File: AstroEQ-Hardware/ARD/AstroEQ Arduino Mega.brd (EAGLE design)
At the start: 101.6 x 53.3 mm, 19 parts, among them J1 POWER_JACKPTH, M0 Motor Driver, M1 Motor Driver

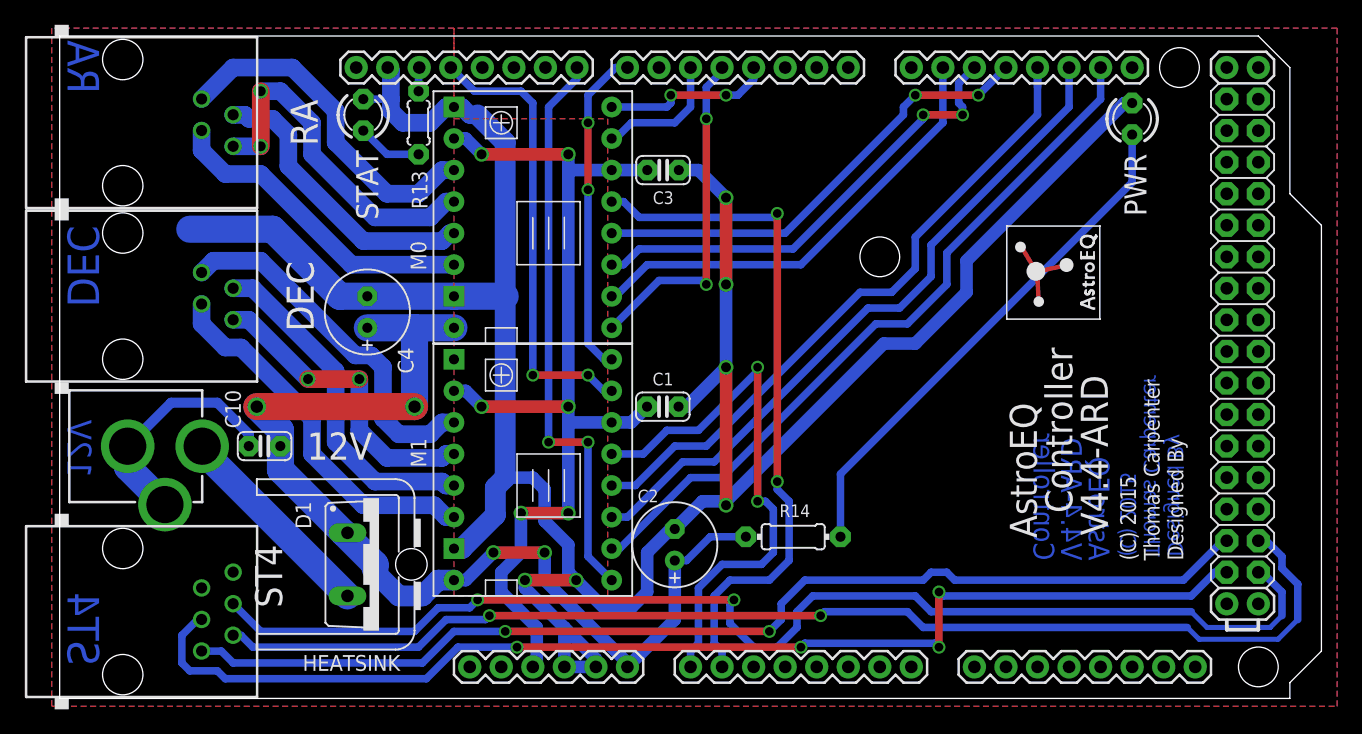
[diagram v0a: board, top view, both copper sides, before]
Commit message: Update Arduino Mega PCB design to V4.8
Adds:
* Speed control line to ST4 connector
* DRV8834 support using 3-pin jumper selection headers.
* PWM output connector jack
* IO header for target speed selection, emergency stop, and snap pin.
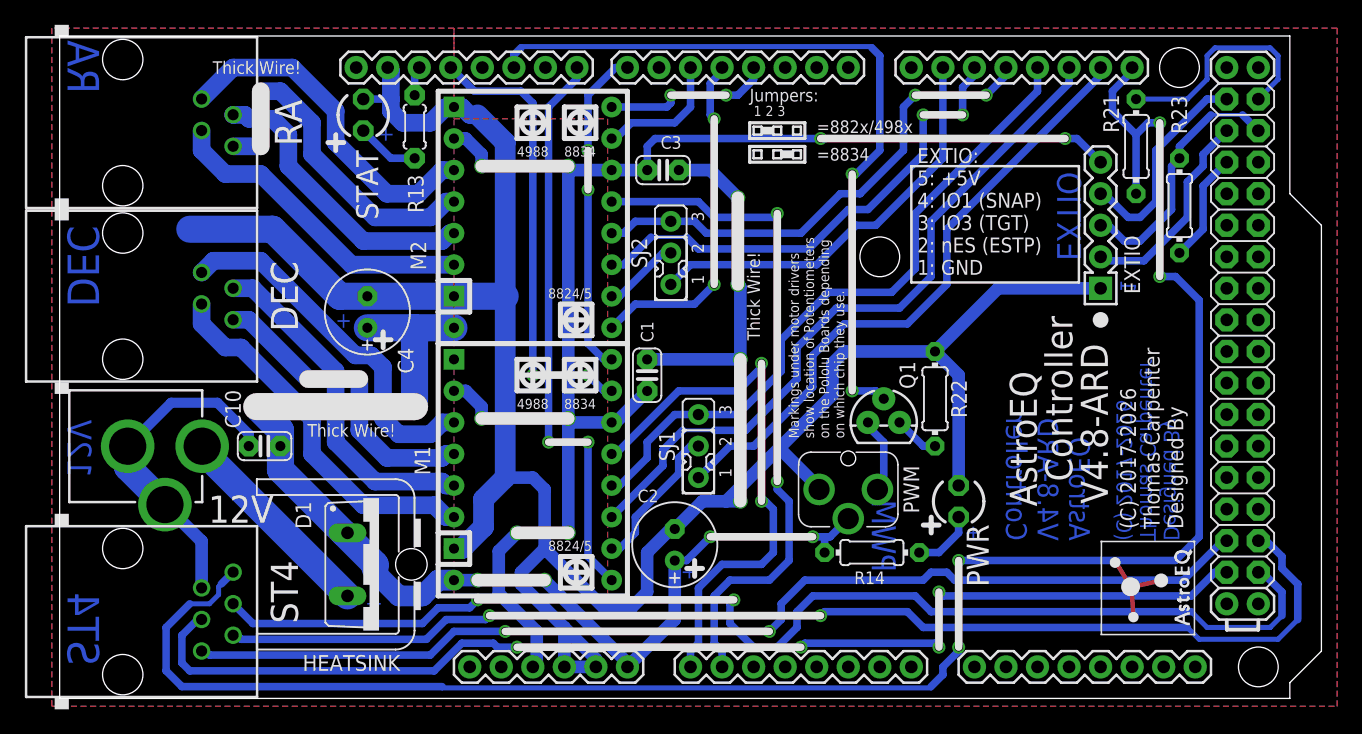
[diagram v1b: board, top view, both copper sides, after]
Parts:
- added EXTIO: 5pin HDR, SparkFun:1X05
- added J2, J3: DNI, jumper:JUMP
- added PWM: JACK, SparkFun:AUDIO-JACK-3.5MM-VERT
- added Q1: BS270, SparkFun:TO-92
- added R21, R23: 1k, rcl:0204/7
- added R22: 120, rcl:0204/7
- added SJ1, SJ2: 3pin HDR, jumper:JP2
- moved PWR 33.8 mm to (72.4, 15.9)
- moved LOGO1 26.5 mm to (91.4, 5.08)
- moved R14 6.47 mm to (65.4, 11.7)
- moved C1 2.83 mm to (47.3, 26.0), turned to 90 degrees
- moved R13 0.45 mm to (28.6, 46.0)
- renumbered M0 to M2
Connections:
- net !EN-0 renamed !EN-2
- net !RST-0 renamed !RST-2
- net DIR-0 renamed DIR-2
- net MS2-0 renamed MS2-2
- net STEP-0 renamed STEP-2
- removed net MS1-0: ARDUINO_MEGA.15, M2.2
- removed net MS3-0: ARDUINO_MEGA.17, M2.4
- new net !ESTOP: ARDUINO_MEGA.24, EXTIO.2
- new net IO0: ARDUINO_MEGA.21, R21.2, ST4.1
- new net IO1: ARDUINO_MEGA.22, EXTIO.4
- new net IO2: ARDUINO_MEGA.23, R21.1
- new net IO3: ARDUINO_MEGA.25, EXTIO.3, R23.2
- new net IO4: ARDUINO_MEGA.26, R23.1
- new net MS1-2: ARDUINO_MEGA.15, SJ2.1
- new net MS13-1: M1.2, SJ1.2
- new net MS13-2: M2.2, SJ2.2
- new net MS3-2: ARDUINO_MEGA.17, M2.4, SJ2.3
- new net PWM: ARDUINO_MEGA.10, Q1.2
- new net PWM-ILIM: Q1.3, R22.2
- new net PWM-OUT: PWM.3, Q1.1
- net +5V: now also EXTIO.5
- net GND: now also EXTIO.1, PWM.1, R22.1
- net MS1-1: now also SJ1.1; no longer M1.2
- net MS3-1: now also SJ1.3
- net V+: now also PWM.2
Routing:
- net IO0: track 0.00 -> 154.0 mm, vias 0 -> 4
- net PWM: track 0.00 -> 62.1 mm, vias 0 -> 2
- net +5V: track 79.8 -> 121.1 mm, vias 6 -> 8
- net MS3-2: track 0.00 -> 40.5 mm, vias 0 -> 2
- net MS3-0: track 37.6 -> 0.00 mm, vias 2 -> 0
- net PWRLED: track 42.1 -> 5.10 mm
- net MS1-0: track 36.9 -> 0.00 mm
- net MS1-2: track 0.00 -> 33.4 mm
- net IO3: track 0.00 -> 20.6 mm
- net GND: track 230.9 -> 249.7 mm, vias 6 -> 4
- net IO2: track 0.00 -> 18.7 mm
- net IO1: track 0.00 -> 17.3 mm
- net !ESTOP: track 0.00 -> 16.9 mm
- net MS13-1: track 0.00 -> 11.9 mm
- net IO4: track 0.00 -> 8.88 mm
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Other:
- outline, holes or cut-outs redrawn
- board text added: "(C) 2017-2026"
- board text added: "+"
- board text added: "1"
- board text added: "1 2 3"
- board text added: "=882x/498x"
- board text added: "=8834"
- board text added: "EXTIO"
- board text added: "EXTIO: 5: +5V 4: IO1 (SNAP) 3: IO3 (TGT) 2: nES (ESTP) 1: GND"
- board text added: "For printing the silkscreen to paper, you should only have TNames, TPlace and Dimension layers visible."
- board text added: "Jumpers:"
- board text added: "PWM"
- board text added: "V4.8-ARD"
- board text removed: "(C) 2015"
- board text removed: "4988"
- board text removed: "8824/5"
- board text removed: "For printing the silkscreen to paper, you should only have TNames, TValues and Dimension layers visible."
- board text removed: "I use iteadstudio.com 10cm x 10cm prototype service, selecting 1.6mm thick, HASL, 100% electrical check"
- board text removed: "Sq Pad"
- board text removed: "V4.4-ARD"
